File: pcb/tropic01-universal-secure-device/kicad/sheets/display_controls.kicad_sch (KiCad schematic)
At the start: 0 parts

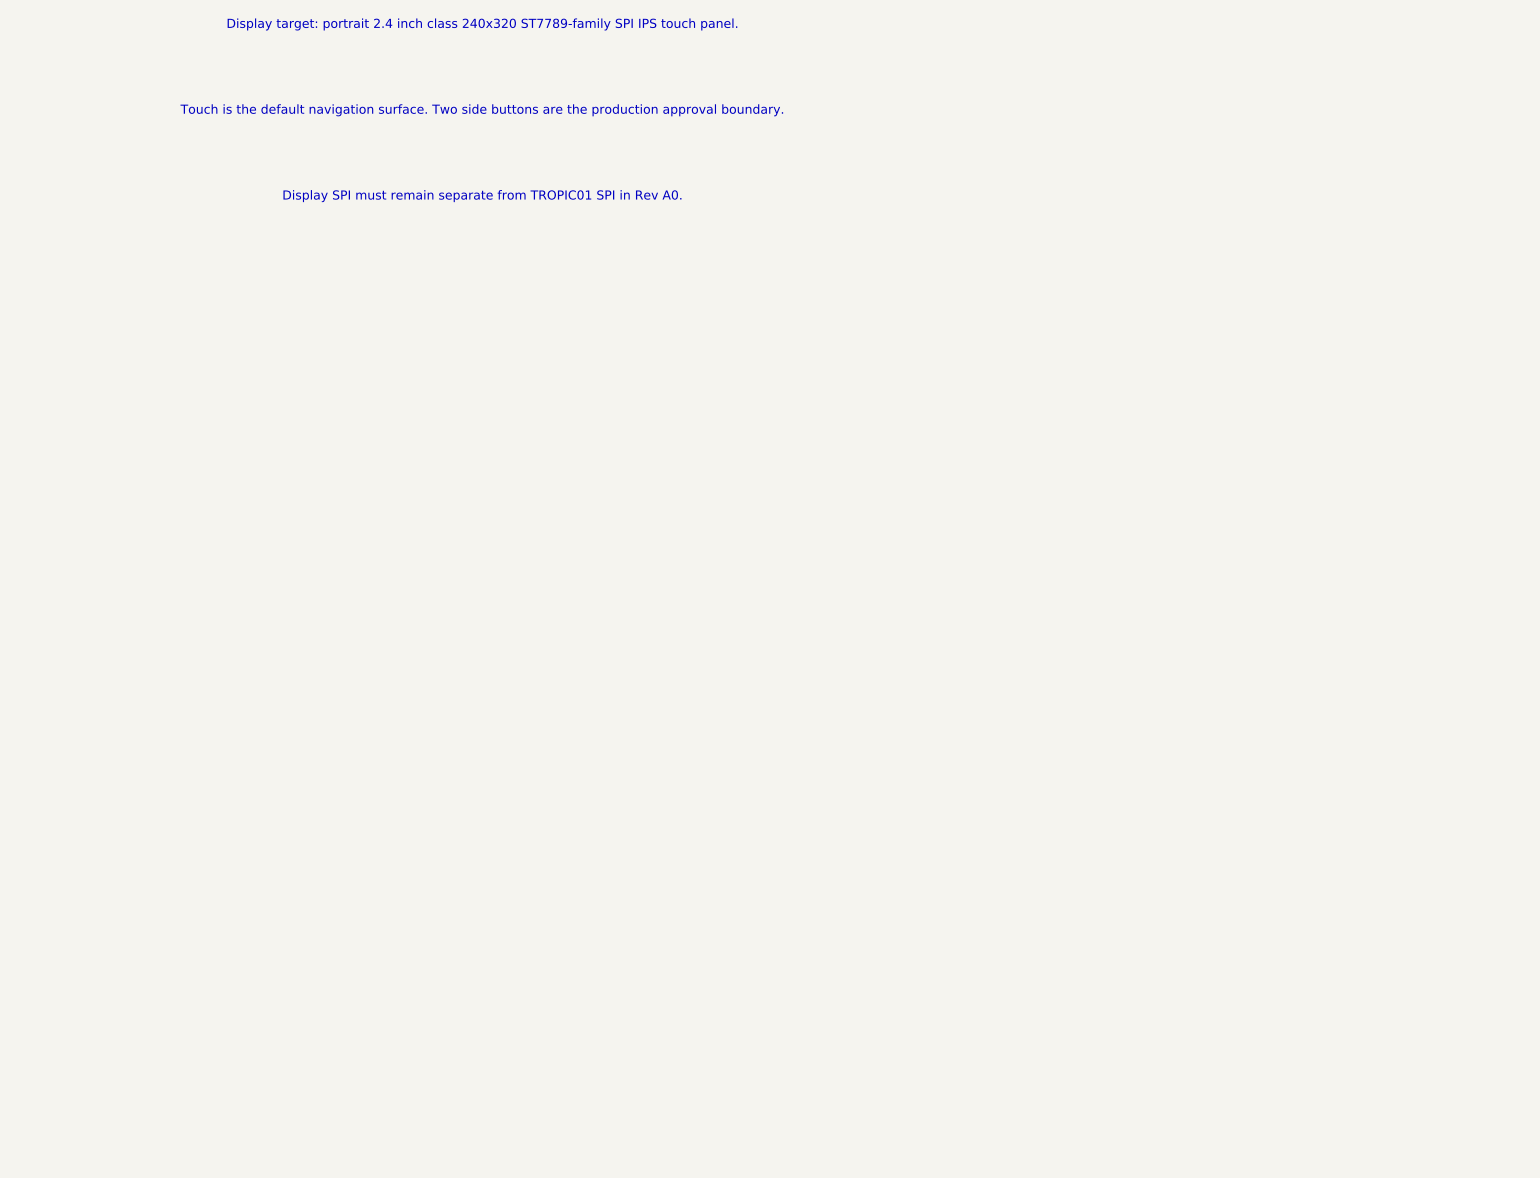
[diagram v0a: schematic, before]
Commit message: feat: materialize tropic01 schematic bindings
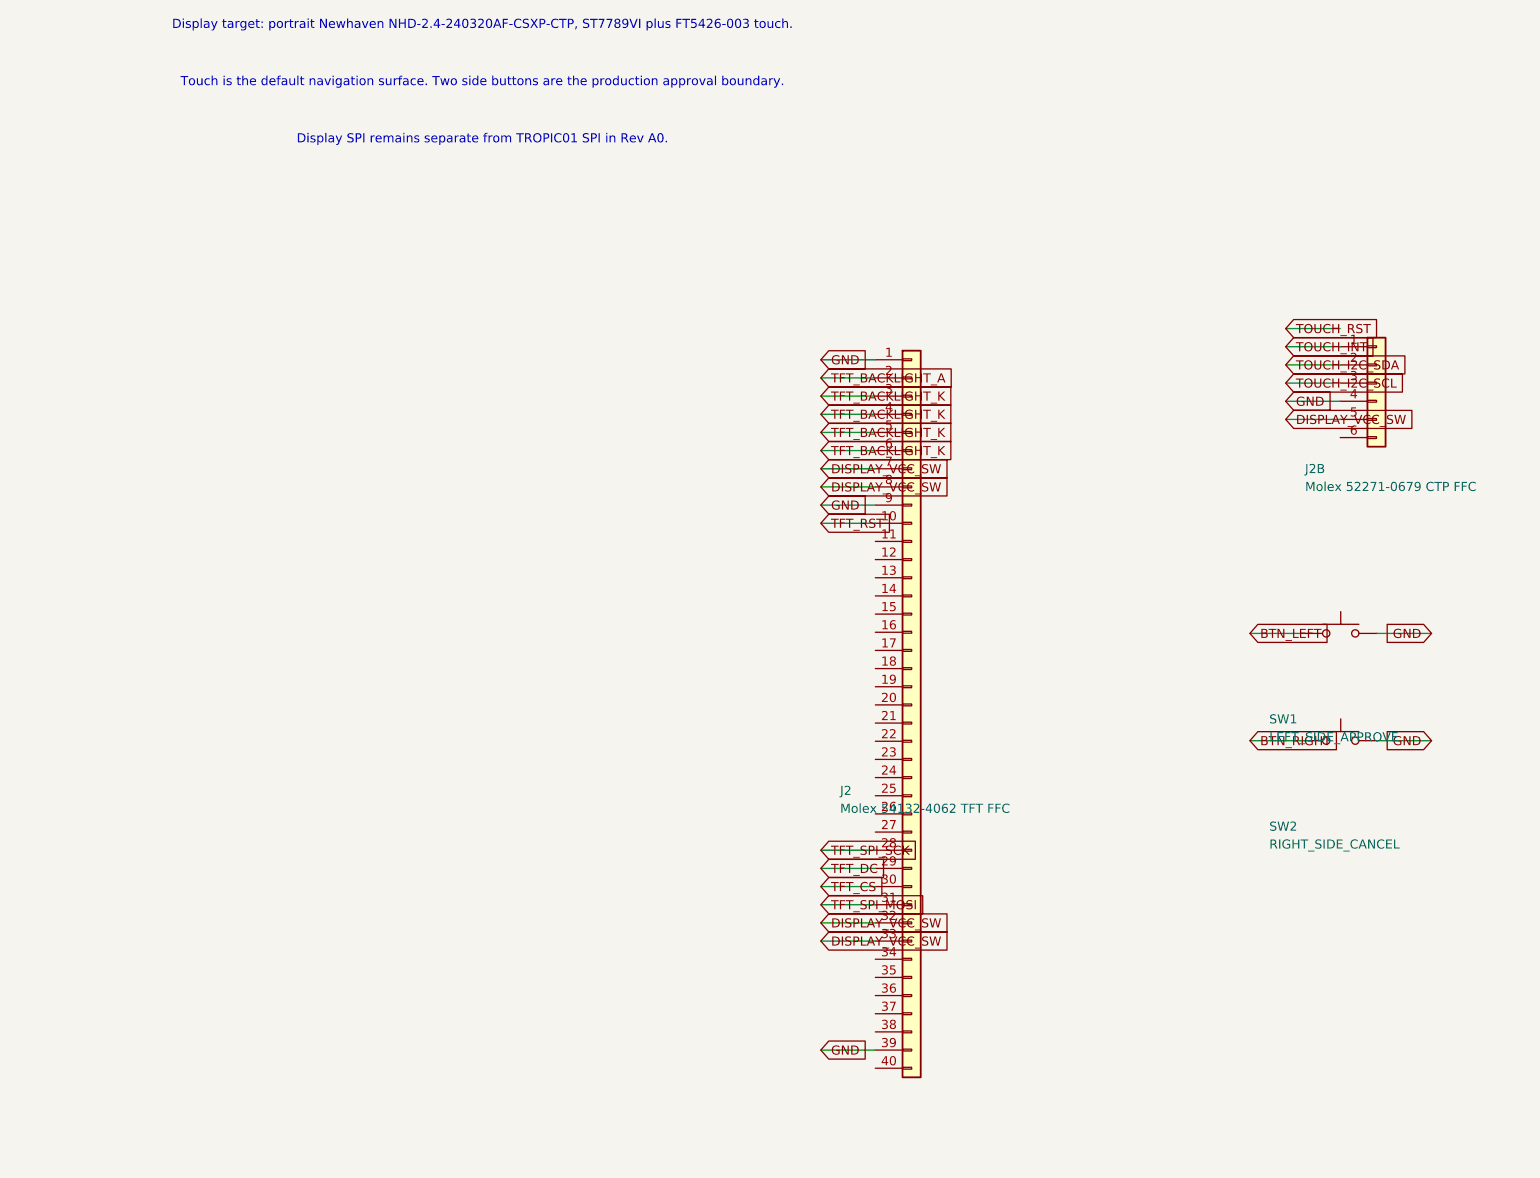
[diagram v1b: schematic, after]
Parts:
- added J2: Molex 54132-4062 TFT FFC, Connector_FFC-FPC:Molex_54132-4062_1x40-1MP_P0.50mm_Horizontal, symbol Connector_Generic:Conn_01x40
- added J2B: Molex 52271-0679 CTP FFC, Connector_FFC-FPC:Molex_52271-0679_1x06-1MP_P1.00mm_Horizontal, symbol Connector_Generic:Conn_01x06
- added SW1: LEFT_SIDE_APPROVE, Button_Switch_SMD:SW_SPST_EVQP7A, symbol Switch:SW_Push
- added SW2: RIGHT_SIDE_CANCEL, Button_Switch_SMD:SW_SPST_EVQP7A, symbol Switch:SW_Push
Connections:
- new net BTN_LEFT: SW1.1
- new net BTN_RIGHT: SW2.1
- new net DISPLAY_VCC_SW: J2.32 (Pin_32), J2.33 (Pin_33), J2.7 (Pin_7), J2.8 (Pin_8), J2B.5 (Pin_5)
- new net GND: J2.1 (Pin_1), J2.39 (Pin_39), J2.9 (Pin_9), J2B.4 (Pin_4), SW1.2, SW2.2
- new net TFT_BACKLIGHT_A: J2.2 (Pin_2)
- new net TFT_BACKLIGHT_K: J2.3 (Pin_3), J2.4 (Pin_4), J2.5 (Pin_5), J2.6 (Pin_6)
- new net TFT_CS: J2.30 (Pin_30)
- new net TFT_DC: J2.29 (Pin_29)
- new net TFT_RST: J2.10 (Pin_10)
- new net TFT_SPI_MOSI: J2.31 (Pin_31)
- new net TFT_SPI_SCK: J2.28 (Pin_28)
- new net TOUCH_I2C_SCL: J2B.3 (Pin_3)
- new net TOUCH_I2C_SDA: J2B.2 (Pin_2)
- new net TOUCH_INT: J2B.1 (Pin_1)
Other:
- note added: "Display SPI remains separate from TROPIC01 SPI in Rev A0."
- note added: "Display target: portrait Newhaven NHD-2.4-240320AF-CSXP-CTP, ST7789VI plus FT5426-003 touch."
- note removed: "Display SPI must remain separate from TROPIC01 SPI in Rev A0."
- note removed: "Display target: portrait 2.4 inch class 240x320 ST7789-family SPI IPS touch panel."

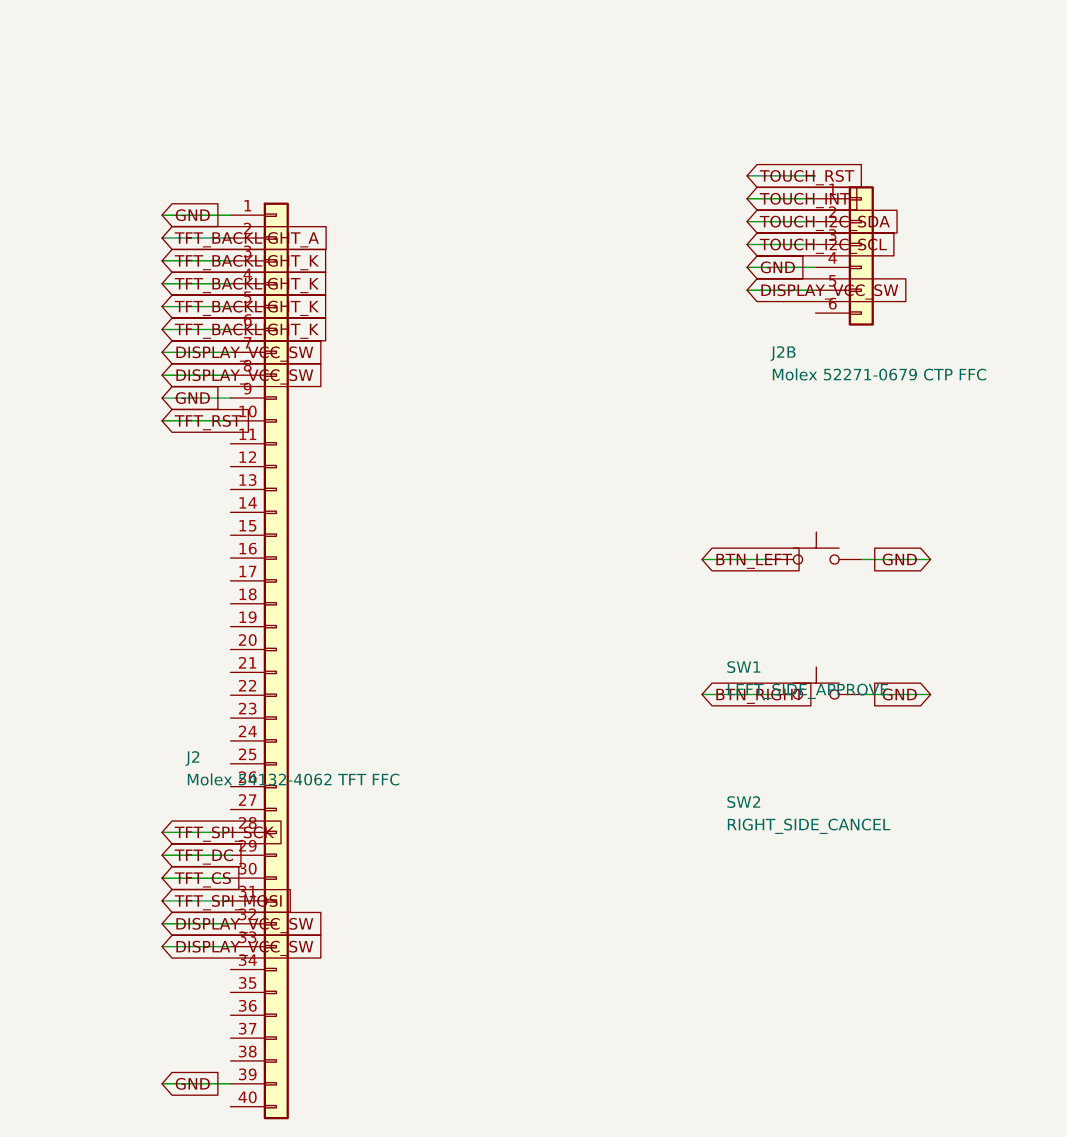
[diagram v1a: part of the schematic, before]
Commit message: feat: bind tropic01 pcb nets
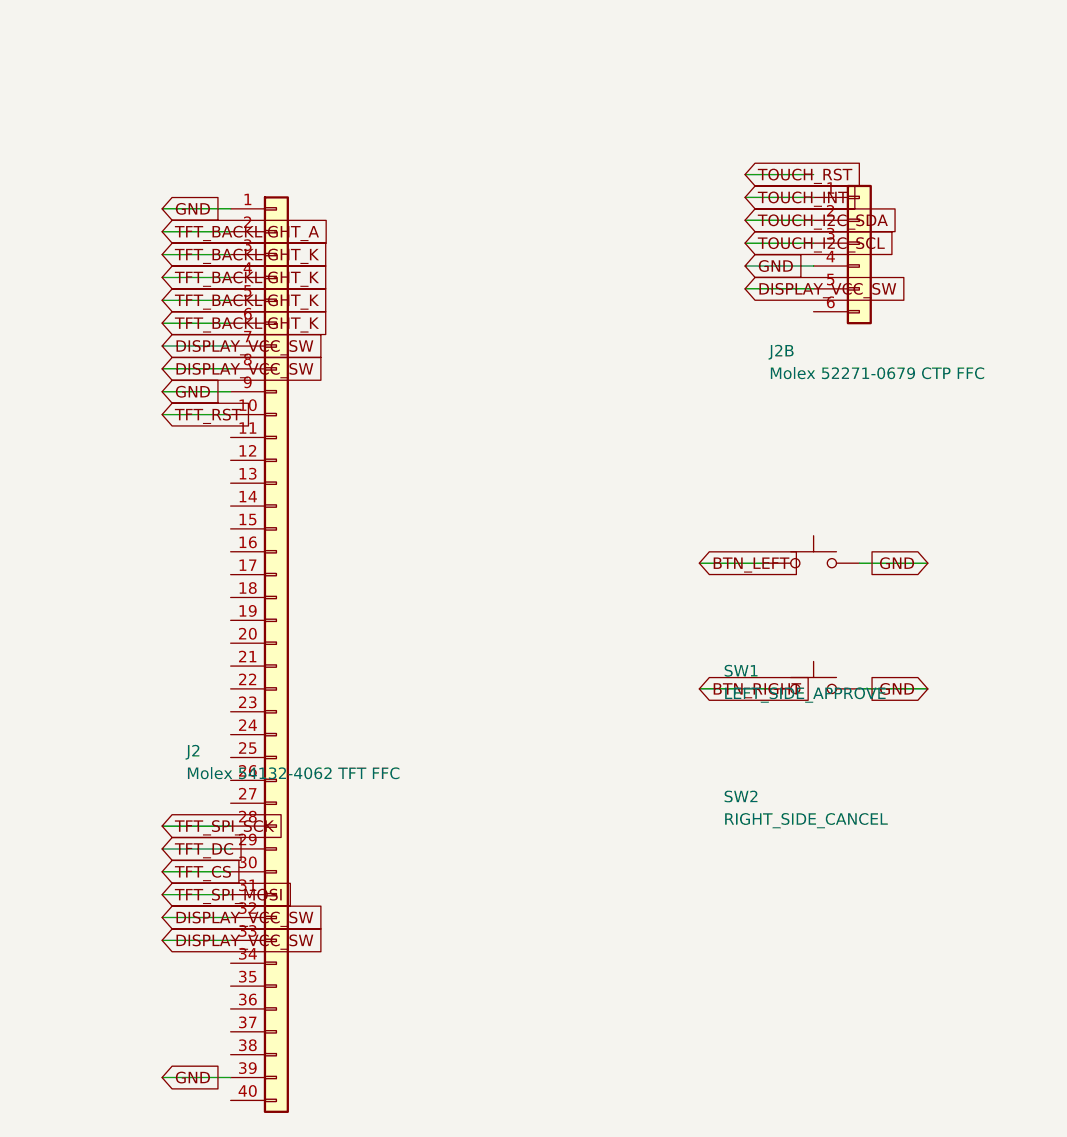
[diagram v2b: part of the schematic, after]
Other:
- moved on the sheet: J2, SW1, SW2
